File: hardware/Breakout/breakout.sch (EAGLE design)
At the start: 14 parts, among them IC1 24AA04SN, IC2 MAX490CSA, X1 VISCA

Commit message: Breakout Board v1
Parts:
- added BI8_SERIAL2: (no value), con-lstb:MA04-2
- added C2: 100nF, SparkFun:CAP0603-CAP
- added CON2: LED2, con-lstb:MA08-1
- added CON5: LED1, con-lstb:MA08-1
- added IC3: MAX490CSA, maxim:MAX488CSA
- added IC4: PCA9685, wsmith:PCA9685
- added R10, R11, R12, R13, R14, R15, R16, R17, R18, R19, R20, R21, R22, R7, R8, R9: 180, SparkFun:RESISTOR0603-RES
- added R3, R4: 120, resistor:R-EU_R0603
- added R5, R6: 10K, resistor:R-EU_R0603
- added SV1: DISPLAY, con-lstb:MA05-2
- added X2: RS485, con-phoenix-350:1751277
- added X3: JOYSTICK, con-ria-59:AKL59-08
- added X4: SLIDER, con-ria-59:AKL59-03
- renumbered BI8_SERIAL to BI8_SERIAL1
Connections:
- new net L0: CON5.1, R22.1
- new net L1: CON5.2, R21.1
- new net L10: CON2.3, R12.1
- new net L11: CON2.4, R11.1
- new net L12: CON2.5, R10.1
- new net L13: CON2.6, R9.1
- new net L14: CON2.7, R8.1
- new net L15: CON2.8, R7.1
- new net L2: CON5.3, R20.1
- new net L3: CON5.4, R19.1
- new net L4: CON5.5, R18.1
- new net L5: CON5.6, R17.1
- new net L6: CON5.7, R16.1
- new net L7: CON5.8, R15.1
- new net L8: CON2.1, R14.1
- new net L9: CON2.2, R13.1
- new net N$10: IC4.L3, R19.2
- new net N$11: IC4.L2, R20.2
- new net N$12: IC4.L1, R21.2
- new net N$19: IC4.L0, R22.2
- new net N$20: IC4.L8, R14.2
- new net N$21: IC4.L9, R13.2
- new net N$22: IC4.L10, R12.2
- new net N$23: IC4.L11, R11.2
- new net N$24: IC4.L12, R10.2
- new net N$25: IC4.L13, R9.2
- new net N$26: IC4.L14, R8.2
- new net N$27: IC4.L15, R7.2
- new net N$4: IC4.L7, R15.2
- new net N$5: IC4.L6, R16.2
- new net N$7: IC4.L5, R17.2
- new net N$9: IC4.L4, R18.2
- new net PD0/DISP_MODE: PD.3, SV1.8
- new net PD1/ENC_INT: PD.4, SV1.10
- new net PD10: PD.13
- new net PD11: PD.14
- new net PD12: PD.15
- new net PD13: PD.16
- new net PD14/JOY_T1: PD.17, R5.2, X3-7.1
- new net PD15/JOY_T2: PD.18, R6.2, X3-8.1
- new net PD3: PD.6
- new net PD4: PD.7
- new net PD7: PD.10
- new net PE0: PE.3
- new net PE1: PE.4
- new net PE10: PE.13
- new net PE11: PE.14
- new net PE12: PE.15
- new net PE13: PE.16
- new net PE14: PE.17
- new net PE15: PE.18
- new net PE2: PE.5
- new net PE3: PE.6
- new net PE4: PE.7
- new net PE5: PE.8
- new net PE6: PE.9
- new net PE7: PE.10
- new net PE8: PE.11
- new net PE9: PE.12
- new net PF12: PF.15
- new net PF13: PF.16
- new net PF14: PF.17
- new net PF15: PF.18
- new net PF2: PF.5
- new net PF3: PF.6
- new net PF4: PF.7
- new net PF5: PF.8
- new net PG0: PG.3
- new net PG1: PG.4
- new net PG12: PG.15
- new net PG15: PG.18
- new net PG2: PG.5
- new net PG3: PG.6
- new net PG4: PG.7
- new net PG5: PG.8
- new net PG6: PG.9
- new net PG7: PG.10
- new net PG8: PG.11
- new net PG9: PG.12
- new net RS485_RXD_N: IC3G$1.B, R4.1, X2-4.K
- new net RS485_RXD_P: IC3G$1.A, R4.2, X2-3.K
- new net RS485_TXD_N: IC3G$1.Z, R3.1, X2-2.K
- new net RS485_TXD_P: IC3G$1.Y, R3.2, X2-1.K
- net A1: now also X4-3.1
- net A2: now also X3-3.1
- net A3: now also X3-4.1
- net A4: now also X3-5.1
- net GND: now also BI8_SERIAL2.1, C2.2, IC3P.GND, IC4.A0, IC4.A1, IC4.A2, IC4.EXTCLK, IC4.GND, IC4.OE, SV1.1, X2-5.K, X3-2.1, X3-6.1, X4-2.1
- net I2C1_SCL: now also BI8_SERIAL2.4
- net I2C1_SDA: now also BI8_SERIAL2.3
- net I2C2_SCL: now also IC4.SCL, SV1.4
- net I2C2_SDA: now also IC4.SDA, SV1.3
- net RST: now also SV1.9
- net SPI1_MOSI: now also SV1.6
- net SPI1_NSS: now also SV1.7
- net SPI1_SCK: now also SV1.5
- net USART3_RX: now also IC3G$1.RO
- net USART3_TX: now also IC3G$1.DI
- net VCC: now also BI8_SERIAL2.2, C2.1, IC3P.VCC, IC4.A3, IC4.A4, IC4.A5, IC4.VDD, R5.1, R6.1, SV1.2, X3-1.1, X4-1.1
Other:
- note added: "ADR=B111000"
- note added: "LED DRIVER"
- moved on the sheet: IC1

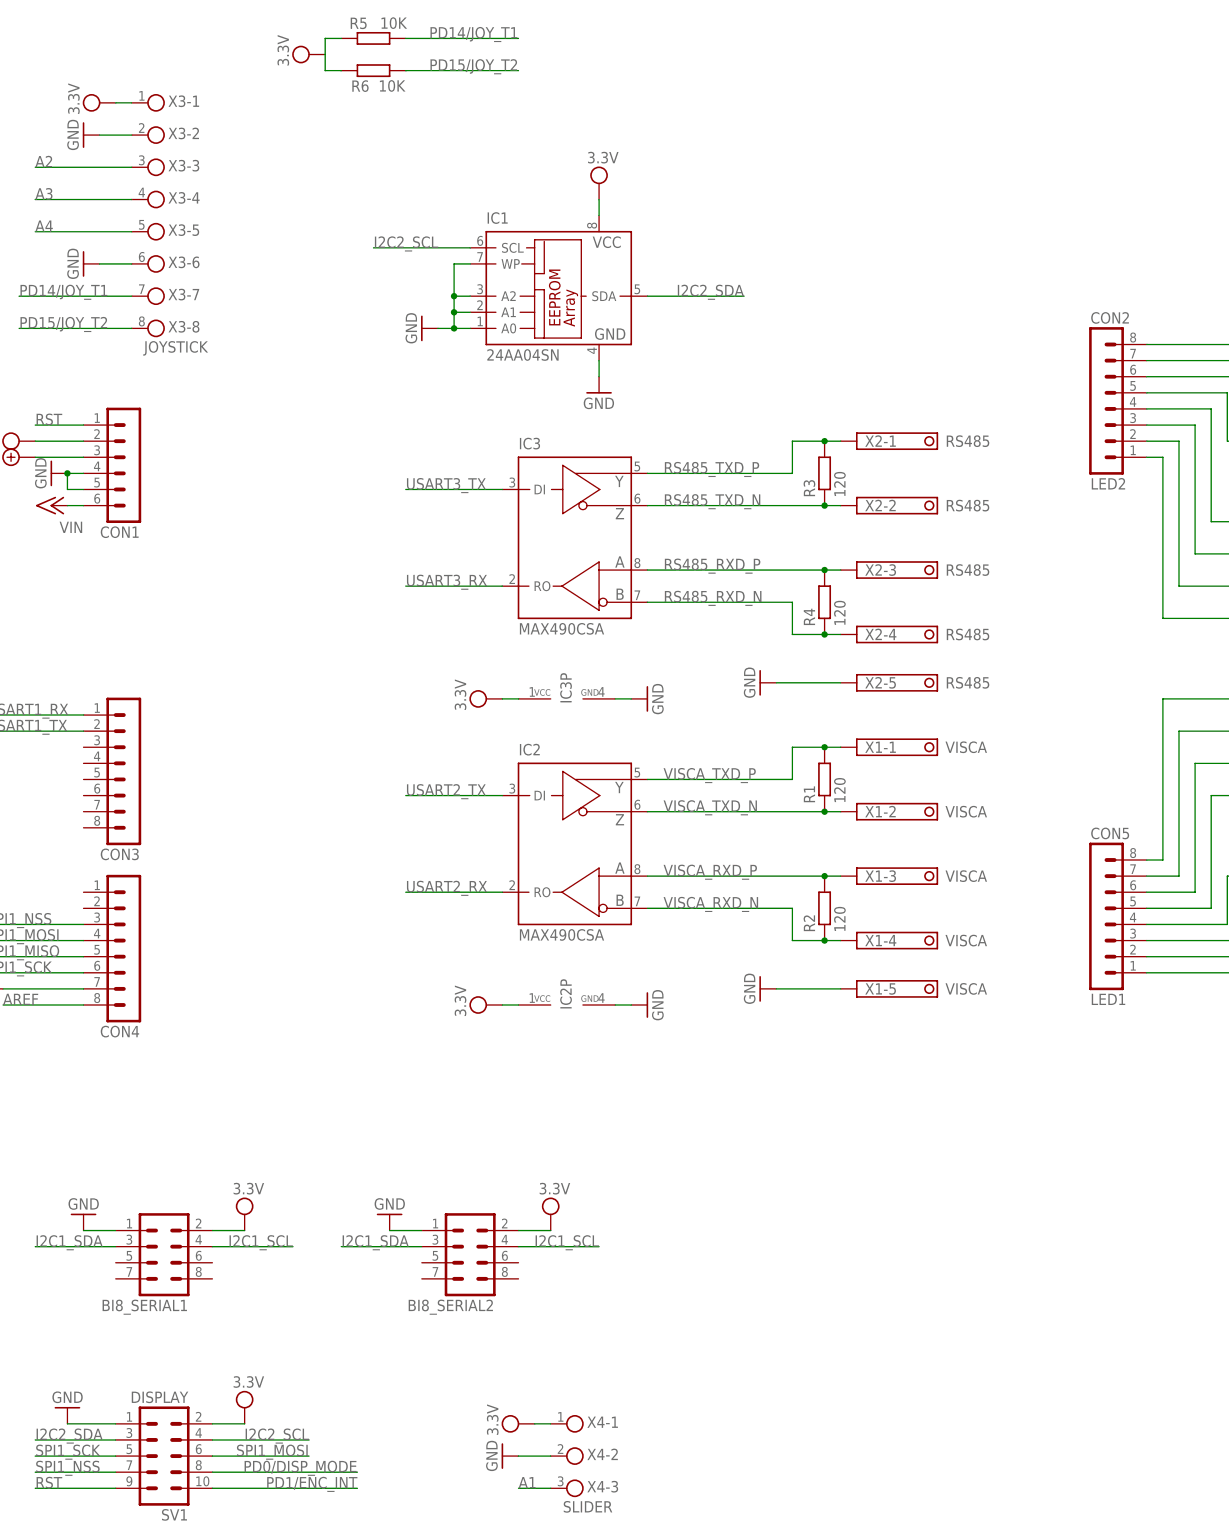
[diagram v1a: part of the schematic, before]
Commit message: Breakout board fixes
Pullups for I2C2, power cycle external boards.
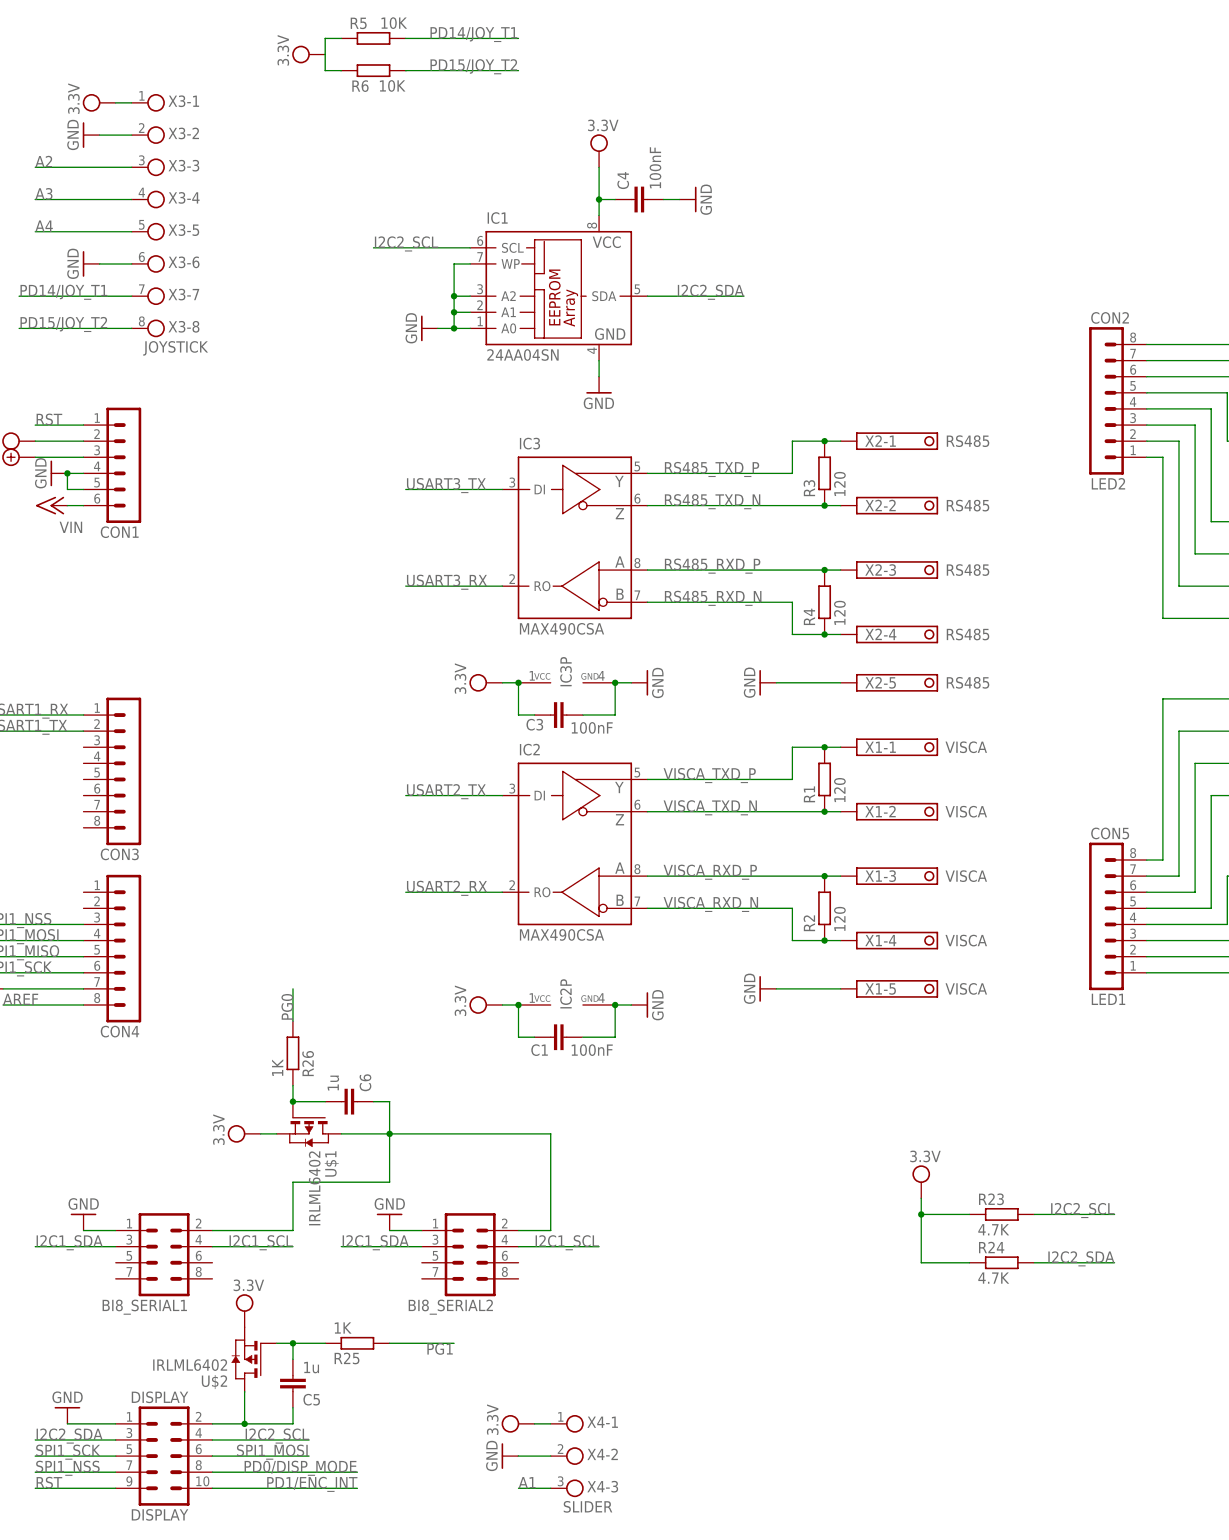
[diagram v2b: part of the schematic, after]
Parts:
- added C1, C3, C4: 100nF, SparkFun:CAP0603-CAP
- added C5, C6: 1u, resistor:C-EUC0805
- added R23, R24: 4.7K, resistor:R-EU_R0603
- added R25, R26: 1K, resistor:R-EU_R0603
- added U$1, U$2: IRLML6402, IRLML6402:IRLML6402
- renumbered SV1 to DISPLAY
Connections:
- new net N$13: C5.1, DISPLAY.2, U$2.D
- new net N$3: C5.2, R25.1, U$2.G
- new net N$6: C6.2, R26.1, U$1.G
- new net N$8: BI8_SERIAL1.2, BI8_SERIAL2.2, C6.1, U$1.D
- net GND: now also C1.2, C3.2, C4.2
- net I2C2_SCL: now also R23.2
- net I2C2_SDA: now also R24.2
- net PG0: now also R26.2
- net PG1: now also R25.2
- net VCC: now also C1.1, C3.1, C4.1, R23.1, R24.1, U$1.S, U$2.S; no longer BI8_SERIAL1.2, BI8_SERIAL2.2, DISPLAY.2
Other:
- moved on the sheet: IC3P

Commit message: Pull-up for SPI2 MOSI (see UEXT on mainboard)
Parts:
- added R27: 47K, resistor:R-EU_R0603
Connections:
- net GND: now also IC4.A3
- net SPI1_MOSI: now also R27.2
- net VCC: now also R27.1; no longer IC4.A3
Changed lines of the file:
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@@
 <?xml version="1.0" encoding="utf-8"?>
 <!DOCTYPE eagle SYSTEM "eagle.dtd">
-<eagle version="6.5.0">
+<eagle version="6.4">
 <drawing>
 <settings>
@@
 <part name="SUPPLY25" library="supply2" deviceset="VCC" device="" value="3.3V"/>
 <part name="SUPPLY15" library="supply2" deviceset="VCC" device="" value="3.3V"/>
+<part name="R27" library="resistor" deviceset="R-EU_" device="R0603" value="47K"/>
 </parts>
 <sheets>
@@
 <instance part="SUPPLY25" gate="G$1" x="106.68" y="-58.42" rot="R90"/>
 <instance part="SUPPLY15" gate="G$1" x="106.68" y="-86.36"/>
+<instance part="R27" gate="G$1" x="226.06" y="-86.36"/>
 </instances>
 <busses>
@@
 <segment>
 <pinref part="IC4" gate="G$1" pin="A4"/>
-<wire x1="342.9" y1="-15.24" x2="340.36" y2="-15.24" width="0.1524" layer="91"/>
 <wire x1="340.36" y1="-15.24" x2="340.36" y2="-12.7" width="0.1524" layer="91"/>
 <pinref part="IC4" gate="G$1" pin="A5"/>
 <wire x1="340.36" y1="-15.24" x2="337.82" y2="-15.24" width="0.1524" layer="91"/>
 <wire x1="337.82" y1="-15.24" x2="337.82" y2="-12.7" width="0.1524" layer="91"/>
-<junction x="340.36" y="-15.24"/>
 <wire x1="337.82" y1="-15.24" x2="335.28" y2="-15.24" width="0.1524" layer="91"/>
 <junction x="337.82" y="-15.24"/>
 <pinref part="SUPPLY23" gate="G$1" pin="VCC"/>
-<pinref part="IC4" gate="G$1" pin="A3"/>
-<wire x1="342.9" y1="-15.24" x2="342.9" y2="-12.7" width="0.1524" layer="91"/>
 </segment>
 <segment>
@@
 <wire x1="213.36" y1="-78.74" x2="220.98" y2="-78.74" width="0.1524" layer="91"/>
 <junction x="213.36" y="-71.12"/>
+<pinref part="R27" gate="G$1" pin="1"/>
+<wire x1="213.36" y1="-78.74" x2="213.36" y2="-86.36" width="0.1524" layer="91"/>
+<wire x1="213.36" y1="-86.36" x2="220.98" y2="-86.36" width="0.1524" layer="91"/>
+<junction x="213.36" y="-78.74"/>
 </segment>
 <segment>
@@
 <junction x="350.52" y="-15.24"/>
 <pinref part="GND25" gate="1" pin="GND"/>
+<pinref part="IC4" gate="G$1" pin="A3"/>
+<wire x1="342.9" y1="-12.7" x2="342.9" y2="-15.24" width="0.1524" layer="91"/>
+<wire x1="342.9" y1="-15.24" x2="345.44" y2="-15.24" width="0.1524" layer="91"/>
+<junction x="345.44" y="-15.24"/>
 </segment>
 <segment>
@@
 <segment>
 <pinref part="PF" gate="G$1" pin="9"/>
-<wire x1="7.62" y1="15.24" x2="0" y2="15.24" width="0.1524" layer="91"/>
-<label x="0" y="15.24" size="1.778" layer="95"/>
+<wire x1="7.62" y1="15.24" x2="-5.08" y2="15.24" width="0.1524" layer="91"/>
+<label x="-5.08" y="15.24" size="1.778" layer="95"/>
 </segment>
 <segment>
@@
 <segment>
 <pinref part="PF" gate="G$1" pin="11"/>
-<wire x1="7.62" y1="12.7" x2="0" y2="12.7" width="0.1524" layer="91"/>
-<label x="0" y="12.7" size="1.778" layer="95"/>
+<wire x1="7.62" y1="12.7" x2="-5.08" y2="12.7" width="0.1524" layer="91"/>
+<label x="-5.08" y="12.7" size="1.778" layer="95"/>
 </segment>
 <segment>
@@
 <segment>
 <pinref part="PF" gate="G$1" pin="10"/>
-<wire x1="22.86" y1="15.24" x2="30.48" y2="15.24" width="0.1524" layer="91"/>
-<label x="27.94" y="15.24" size="1.778" layer="95"/>
+<wire x1="22.86" y1="15.24" x2="38.1" y2="15.24" width="0.1524" layer="91"/>
+<label x="38.1" y="15.24" size="1.778" layer="95" rot="MR0"/>
 </segment>
 <segment>
@@
 <segment>
 <pinref part="PF" gate="G$1" pin="12"/>
-<wire x1="22.86" y1="12.7" x2="30.48" y2="12.7" width="0.1524" layer="91"/>
-<label x="27.94" y="12.7" size="1.778" layer="95"/>
+<wire x1="22.86" y1="12.7" x2="38.1" y2="12.7" width="0.1524" layer="91"/>
+<label x="38.1" y="12.7" size="1.778" layer="95" rot="MR0"/>
 </segment>
 <segment>
@@
 <segment>
 <pinref part="PF" gate="G$1" pin="13"/>
-<wire x1="7.62" y1="10.16" x2="0" y2="10.16" width="0.1524" layer="91"/>
-<label x="0" y="10.16" size="1.778" layer="95"/>
+<wire x1="7.62" y1="10.16" x2="-5.08" y2="10.16" width="0.1524" layer="91"/>
+<label x="-5.08" y="10.16" size="1.778" layer="95"/>
 </segment>
 </net>
@@
 <label x="116.84" y="-109.22" size="1.778" layer="95" rot="MR0"/>
 </segment>
-</net>
+<segment>
+<pinref part="R27" gate="G$1" pin="2"/>
+<wire x1="231.14" y1="-86.36" x2="243.84" y2="-86.36" width="0.1524" layer="91"/>
+<label x="243.84" y="-86.36" size="1.778" layer="95" rot="MR0"/>
+</segment>
+</net>
